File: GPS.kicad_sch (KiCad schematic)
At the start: 14 parts, among them J69 67800-8005, J70 Conn_01x05, U12 AMS1117-3.3, U42 2.54mm 1x6 socket, U43 2.54mm 1x8 socket, U44 2.54mm 1x8 socket, U45 2.54mm 1x10 socket, U46 2.54mm 2x6 socket

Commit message: wip
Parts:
- added D25: LED GREEN, LED_SMD:LED_0805_2012Metric, symbol Device:LED
- added R44: 1k, Resistor_SMD:R_0805_2012Metric, symbol Device:R
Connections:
- net 5V: now also D25.2 (A)
- net GND: now also R44.2
- new net: D25.1 (K), R44.1

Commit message: wip
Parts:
- J69: JLC (none) -> C7500843
- J70: now not fitted
- U12: JLC (none) -> C6186

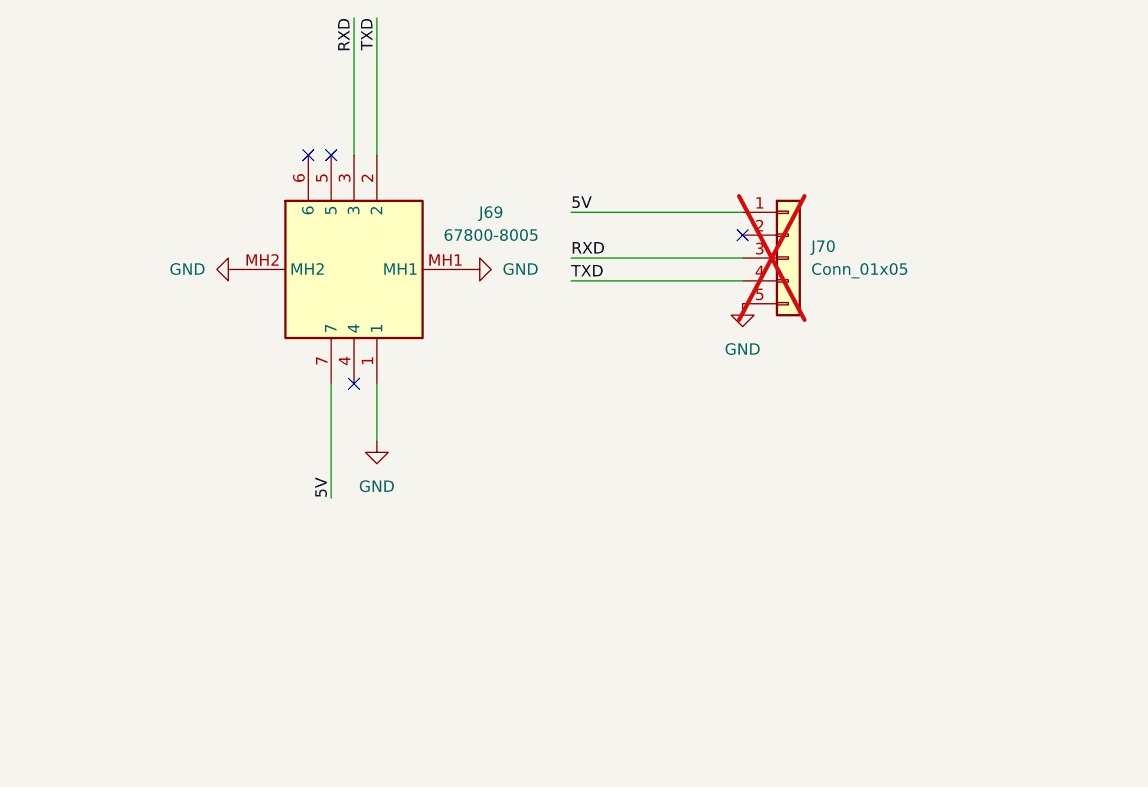
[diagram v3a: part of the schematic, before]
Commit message: Switched SATA to XH connectors
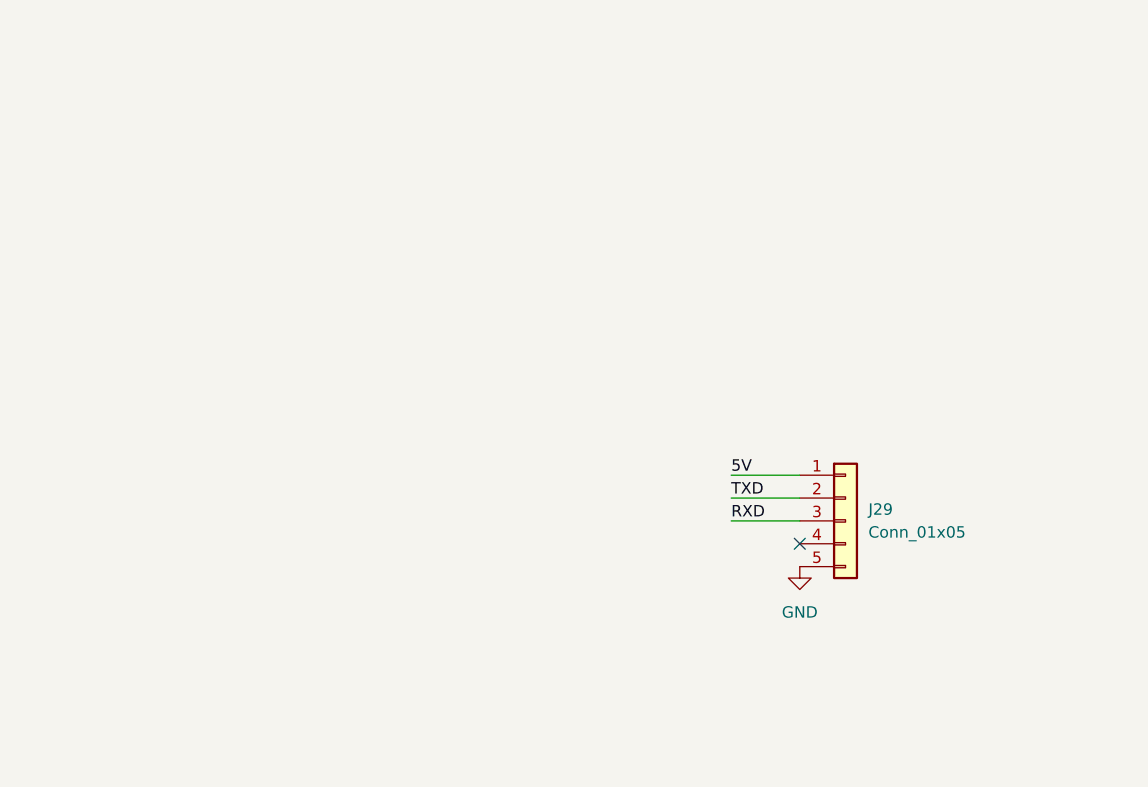
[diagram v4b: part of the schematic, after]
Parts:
- removed J69: 67800-8005, SATA-Molex-67800-8005:SATA-Molex-67800-8005, symbol SATA-Molex-67800-8005:67800-8005
- removed J70: Conn_01x05, Connector_PinHeader_2.54mm:PinHeader_1x05_P2.54mm_Vertical, symbol Connector_Generic:Conn_01x05
- added J29: Conn_01x05, Connector_JST:JST_XH_B5B-XH-A_1x05_P2.50mm_Vertical, symbol Connector_Generic:Conn_01x05
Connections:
- net 5V: now also J29.1 (Pin_1)
- net GND: now also J29.5 (Pin_5)
- net RXD: now also J29.3 (Pin_3)
- net TXD: now also J29.2 (Pin_2)
- no-connect marks 4 -> 1

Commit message: Fixed BOM
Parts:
- J29: JLC (none) -> C157991
